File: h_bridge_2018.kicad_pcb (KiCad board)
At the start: 2 copper layers, 12 parts, among them J1 U$4, J2 Alim puissance, J7 PWM input, U1 LMD18200

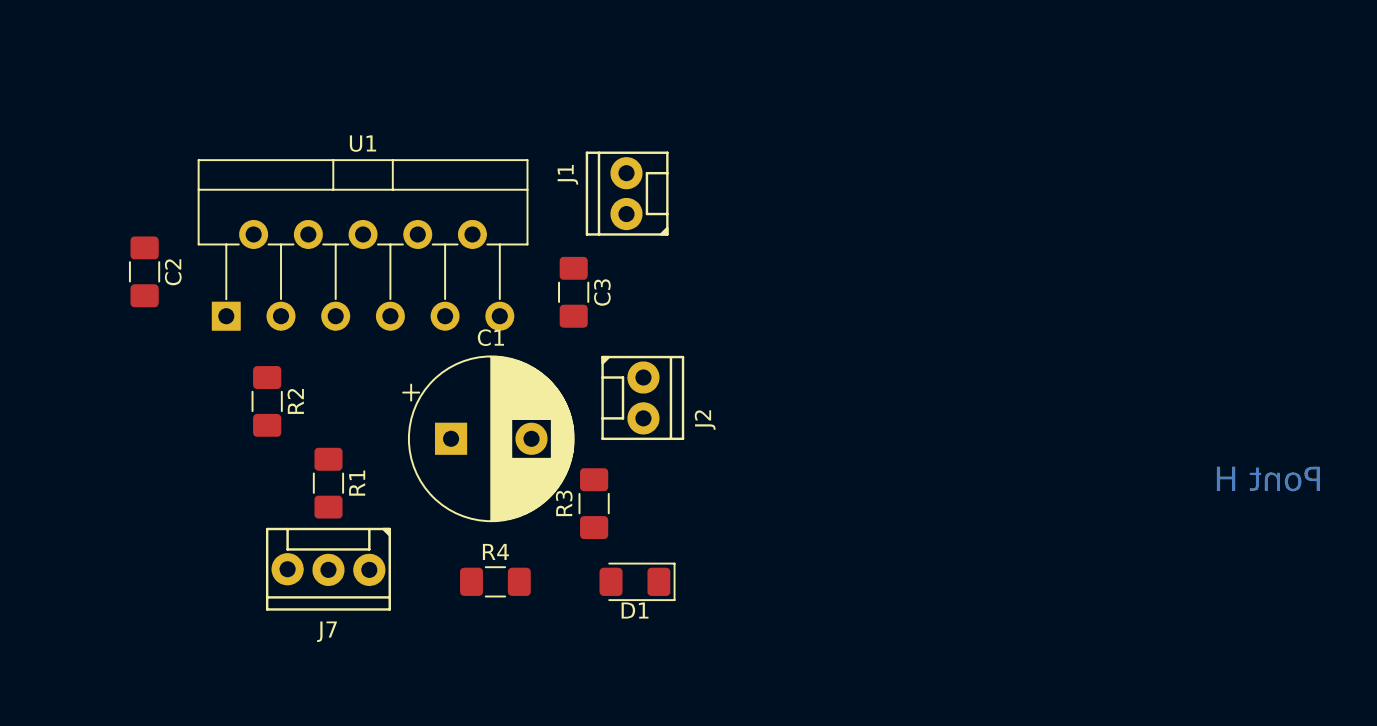
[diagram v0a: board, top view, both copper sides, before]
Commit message: h_bridge modified version
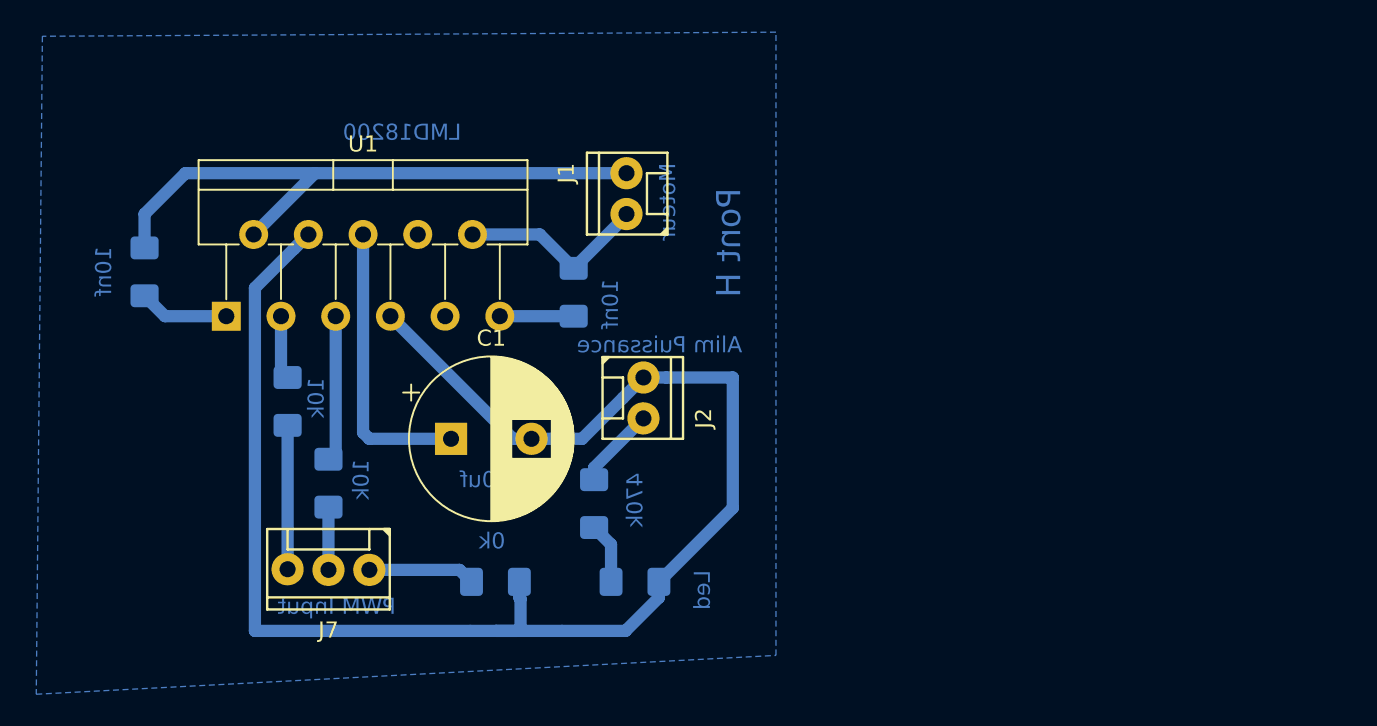
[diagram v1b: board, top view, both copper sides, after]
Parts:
- C2, C3, D1, R1, R2, R3, R4: moved to B.Cu
- moved R2 1.27 mm to (144.8, 84.0)
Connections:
- C1 pad 1: (no net) -> Net-(C1-Pad1)
- C1 pad 2: (no net) -> GNDPWR
- C2 pad 1: (no net) -> Net-(C2-Pad1)
- C2 pad 2: (no net) -> Net-(C2-Pad2)
- C3 pad 1: (no net) -> Net-(C3-Pad1)
- C3 pad 2: (no net) -> Net-(C3-Pad2)
- D1 pad 1: (no net) -> GNDPWR
- D1 pad 2: (no net) -> Net-(D1-Pad2)
- J1 pad 1: (no net) -> Net-(C3-Pad1)
- J1 pad 2: (no net) -> Net-(C2-Pad1)
- J2 pad 1: (no net) -> GNDPWR
- J2 pad 2: (no net) -> /VS
- J7 pad 1: (no net) -> Net-(J7-Pad1)
- J7 pad 2: (no net) -> Net-(J7-Pad2)
- J7 pad 3: (no net) -> Net-(J7-Pad3)
- R1 pad 1: (no net) -> Net-(R1-Pad1)
- R1 pad 2: (no net) -> Net-(J7-Pad2)
- R2 pad 1: (no net) -> Net-(R2-Pad1)
- R2 pad 2: (no net) -> Net-(J7-Pad3)
- R3 pad 1: (no net) -> Net-(D1-Pad2)
- R3 pad 2: (no net) -> /VS
- R4 pad 1: (no net) -> Net-(J7-Pad1)
- R4 pad 2: (no net) -> GNDPWR
- U1 pad 1: (no net) -> Net-(C2-Pad2)
- U1 pad 10: (no net) -> Net-(C3-Pad1)
- U1 pad 11: (no net) -> Net-(C3-Pad2)
- U1 pad 2: (no net) -> Net-(C2-Pad1)
- U1 pad 3: (no net) -> Net-(R2-Pad1)
- U1 pad 4: (no net) -> GNDPWR
- U1 pad 5: (no net) -> Net-(R1-Pad1)
- U1 pad 6: (no net) -> Net-(C1-Pad1)
- U1 pad 7: (no net) -> GNDPWR
- U1 pad 8: (no net) -> Net-(U1-Pad8)
- U1 pad 9: (no net) -> Net-(U1-Pad9)
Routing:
- net GNDPWR: track 0.00 -> 99.2 mm
- net Net-(C2-Pad1): track 0.00 -> 38.5 mm
- net Net-(C1-Pad1): track 0.00 -> 17.9 mm
- net Net-(C3-Pad1): track 0.00 -> 13.1 mm
- net Net-(R1-Pad1): track 0.00 -> 9.08 mm
- net Net-(J7-Pad3): track 0.00 -> 8.94 mm
- net Net-(J7-Pad1): track 0.00 -> 6.66 mm
- net Net-(C2-Pad2): track 0.00 -> 5.61 mm
- net /VS: track 0.00 -> 5.08 mm
- net Net-(C3-Pad2): track 0.00 -> 4.59 mm
- net Net-(R2-Pad1): track 0.00 -> 3.98 mm
- net Net-(J7-Pad2): track 0.00 -> 3.90 mm
- net Net-(D1-Pad2): track 0.00 -> 3.81 mm
- added copper zone on B.Cu, net GNDPWR
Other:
- board text added: "0k"
- board text added: "10k"
- board text added: "10nf"
- board text added: "470k"
- board text added: "470uf"
- board text added: "Alim Puissance"
- board text added: "LMD18200"
- board text added: "Led"
- board text added: "Moteur"
- board text added: "PWM Input"

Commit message: Update h_bridge_2018.kicad_pcb
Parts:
- moved C1 1.27 mm to (154.9, 85.1)
- moved C2 1.20 mm to (137.1, 76.0)
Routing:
- net GNDPWR: track 99.2 -> 102.2 mm
- net Net-(C2-Pad2): track 5.61 -> 4.40 mm
- net Net-(C1-Pad1): track 17.9 -> 16.9 mm
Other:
- board text removed: "0k"
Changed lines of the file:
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@@
   (general
     (thickness 1.6)
-    (drawings 13)
+    (drawings 12)
     (tracks 52)
     (zones 0)
@@
   )
   (module Capacitor_SMD:C_1206_3216Metric_Pad1.42x1.75mm_HandSolder (layer B.Cu)
-    (at 135.89 75.9825 270)
+    (at 137.09396 75.99172 270)
     (descr "Capacitor SMD 1206 (3216 Metric), square (rectangular) end terminal, IPC_7351 nominal with elongated pad for handsoldering. (Body size source: http://www.tortai-tech.com/upload/download/2011102023233369053.pdf), generated with kicad-footprint-generator")
     (tags "capacitor handsolder")
@@
   )
   (module Capacitor_THT:CP_Radial_D10.0mm_P5.00mm (layer F.Cu)
-    (at 154.94 86.36)
+    (at 154.94 85.09)
     (descr "CP, Radial series, Radial, pin pitch=5.00mm, , diameter=10mm, Electrolytic Capacitor")
     (tags "CP Radial series Radial pin pitch 5.00mm  diameter 10mm Electrolytic Capacitor")
@@
     )
   )
-  (gr_text Moteur (at 168.402 71.628 90) (layer B.Cu)
-    (effects (font (size 1 1) (thickness 0.1)) (justify mirror))
-  )
-  (gr_text "470k\n" (at 166.37 90.17 90) (layer B.Cu)
-    (effects (font (size 1 1) (thickness 0.1)) (justify mirror))
-  )
-  (gr_text "0k\n" (at 157.48 92.71) (layer B.Cu)
-    (effects (font (size 1 1) (thickness 0.1)) (justify mirror))
-  )
-  (gr_text "Led " (at 170.561 95.758 90) (layer B.Cu)
-    (effects (font (size 1 1) (thickness 0.1)) (justify mirror))
-  )
-  (gr_text "Alim Puissance" (at 167.894 80.518) (layer B.Cu)
-    (effects (font (size 1 1) (thickness 0.1)) (justify mirror))
-  )
-  (gr_text 10nf (at 164.846 77.978 90) (layer B.Cu)
-    (effects (font (size 1 1) (thickness 0.1)) (justify mirror))
-  )
-  (gr_text "10nf\n" (at 133.35 75.946 90) (layer B.Cu)
-    (effects (font (size 1 1) (thickness 0.1)) (justify mirror))
-  )
-  (gr_text "10k\n" (at 149.352 88.9 90) (layer B.Cu)
+  (gr_text Moteur (at 168.91 71.12 90) (layer B.Cu)
+    (effects (font (size 1 1) (thickness 0.1)) (justify mirror))
+  )
+  (gr_text "470k\n" (at 167.005 90.17 90) (layer B.Cu)
+    (effects (font (size 1 1) (thickness 0.1)) (justify mirror))
+  )
+  (gr_text "Led " (at 170.815 95.758 90) (layer B.Cu)
+    (effects (font (size 1 1) (thickness 0.1)) (justify mirror))
+  )
+  (gr_text "Alim Puissance" (at 175.26 86.36 90) (layer B.Cu)
+    (effects (font (size 1 1) (thickness 0.1)) (justify mirror))
+  )
+  (gr_text 10nf (at 166.37 77.25156 90) (layer B.Cu)
+    (effects (font (size 1 1) (thickness 0.1)) (justify mirror))
+  )
+  (gr_text "10nf\n" (at 133.985 76.01712 90) (layer B.Cu)
+    (effects (font (size 1 1) (thickness 0.1)) (justify mirror))
+  )
+  (gr_text "10k\n" (at 150.495 88.9 90) (layer B.Cu)
     (effects (font (size 1 1) (thickness 0.1)) (justify mirror))
   )
@@
     (effects (font (size 1 1) (thickness 0.1)) (justify mirror))
   )
-  (gr_text 470uf (at 157.48 88.9) (layer B.Cu)
-    (effects (font (size 1 1) (thickness 0.1)) (justify mirror))
-  )
-  (gr_text "LMD18200\n" (at 151.892 67.31) (layer B.Cu)
-    (effects (font (size 1 1) (thickness 0.1)) (justify mirror))
-  )
-  (gr_text "Pont H" (at 172.212 74.168 90) (layer B.Cu)
+  (gr_text 470uf (at 157.48 88.265) (layer B.Cu)
+    (effects (font (size 1 1) (thickness 0.1)) (justify mirror))
+  )
+  (gr_text "LMD18200\n" (at 153.53284 67.31) (layer B.Cu)
+    (effects (font (size 1 1) (thickness 0.1)) (justify mirror))
+  )
+  (gr_text "Pont H" (at 172.72 74.10704 90) (layer B.Cu)
     (effects (font (size 1.5 1.5) (thickness 0.3)) (justify mirror))
   )
-  (segment (start 156.27 73.66) (end 157.48 73.66) (width 0.25) (layer B.Cu) (net 5))
-  (segment (start 147.77 87.18) (end 147.32 87.63) (width 0.762) (layer B.Cu) (net 12))
-  (segment (start 147.77 78.74) (end 147.77 87.18) (width 0.762) (layer B.Cu) (net 12))
-  (segment (start 147.32 90.605) (end 147.32 94.506253) (width 0.762) (layer B.Cu) (net 10))
-  (segment (start 146.48 69.85) (end 142.67 73.66) (width 0.762) (layer B.Cu) (net 4))
-  (segment (start 165.843747 69.85) (end 146.48 69.85) (width 0.762) (layer B.Cu) (net 4))
-  (segment (start 157.97 78.74) (end 162.56 78.74) (width 0.762) (layer B.Cu) (net 6))
-  (segment (start 160.455 73.66) (end 162.56 75.765) (width 0.762) (layer B.Cu) (net 5))
-  (segment (start 156.27 73.66) (end 160.455 73.66) (width 0.762) (layer B.Cu) (net 5))
-  (segment (start 165.843747 72.481253) (end 162.56 75.765) (width 0.762) (layer B.Cu) (net 5))
-  (segment (start 165.843747 72.39) (end 165.843747 72.481253) (width 0.762) (layer B.Cu) (net 5))
-  (segment (start 137.16 78.74) (end 135.89 77.47) (width 0.762) (layer B.Cu) (net 3))
-  (segment (start 140.97 78.74) (end 137.16 78.74) (width 0.762) (layer B.Cu) (net 3))
-  (segment (start 135.89 74.495) (end 135.89 72.39) (width 0.762) (layer B.Cu) (net 4))
-  (segment (start 138.43 69.85) (end 146.48 69.85) (width 0.762) (layer B.Cu) (net 4))
-  (segment (start 135.89 72.39) (end 138.43 69.85) (width 0.762) (layer B.Cu) (net 4))
-  (segment (start 155.466253 94.506253) (end 156.21 95.25) (width 0.762) (layer B.Cu) (net 9))
-  (segment (start 149.86 94.506253) (end 155.466253 94.506253) (width 0.762) (layer B.Cu) (net 9))
-  (segment (start 149.47 73.66) (end 149.47 85.97) (width 0.762) (layer B.Cu) (net 2))
-  (segment (start 149.86 86.36) (end 154.94 86.36) (width 0.762) (layer B.Cu) (net 2))
-  (segment (start 149.47 85.97) (end 149.86 86.36) (width 0.762) (layer B.Cu) (net 2))
-  (segment (start 158.79 86.36) (end 159.94 86.36) (width 0.762) (layer B.Cu) (net 1))
-  (segment (start 151.17 78.74) (end 158.79 86.36) (width 0.762) (layer B.Cu) (net 1))
-  (segment (start 159.94 86.36) (end 163.086253 86.36) (width 0.762) (layer B.Cu) (net 1))
   (segment (start 165.626253 83.82) (end 166.896253 82.55) (width 0.762) (layer B.Cu) (net 1))
-  (segment (start 163.086253 86.36) (end 165.626253 83.82) (width 0.762) (layer B.Cu) (net 1))
-  (segment (start 163.83 88.156253) (end 166.896253 85.09) (width 0.762) (layer B.Cu) (net 8))
-  (segment (start 163.83 88.9) (end 163.83 88.156253) (width 0.762) (layer B.Cu) (net 8))
-  (segment (start 144.37 82.14) (end 144.78 82.55) (width 0.762) (layer B.Cu) (net 13))
-  (segment (start 144.37 78.74) (end 144.37 82.14) (width 0.762) (layer B.Cu) (net 13))
-  (segment (start 144.78 85.525) (end 144.78 94.466253) (width 0.762) (layer B.Cu) (net 11))
   (segment (start 145.170001 74.559999) (end 145.150001 74.559999) (width 0.762) (layer B.Cu) (net 1))
   (segment (start 146.07 73.66) (end 145.170001 74.559999) (width 0.762) (layer B.Cu) (net 1))
@@
   (segment (start 167.8575 96.225) (end 165.7845 98.298) (width 0.762) (layer B.Cu) (net 1))
   (segment (start 167.8575 95.25) (end 167.8575 96.225) (width 0.762) (layer B.Cu) (net 1))
+  (segment (start 151.17 78.74) (end 151.17 82.51) (width 0.762) (layer B.Cu) (net 1))
+  (segment (start 157.36 82.51) (end 159.94 85.09) (width 0.762) (layer B.Cu) (net 1))
+  (segment (start 151.17 82.51) (end 157.36 82.51) (width 0.762) (layer B.Cu) (net 1))
+  (segment (start 164.356253 85.09) (end 166.896253 82.55) (width 0.762) (layer B.Cu) (net 1))
+  (segment (start 159.94 85.09) (end 164.356253 85.09) (width 0.762) (layer B.Cu) (net 1))
+  (segment (start 149.47 85.09) (end 154.94 85.09) (width 0.762) (layer B.Cu) (net 2))
+  (segment (start 149.47 73.66) (end 149.47 85.09) (width 0.762) (layer B.Cu) (net 2))
+  (segment (start 139.70922 77.47922) (end 140.97 78.74) (width 0.762) (layer B.Cu) (net 3))
+  (segment (start 137.09396 77.47922) (end 139.70922 77.47922) (width 0.762) (layer B.Cu) (net 3))
+  (segment (start 146.48 69.85) (end 142.67 73.66) (width 0.762) (layer B.Cu) (net 4))
+  (segment (start 165.843747 69.85) (end 146.48 69.85) (width 0.762) (layer B.Cu) (net 4))
+  (segment (start 138.43 69.85) (end 146.48 69.85) (width 0.762) (layer B.Cu) (net 4))
+  (segment (start 137.09396 74.50422) (end 137.09396 71.18604) (width 0.762) (layer B.Cu) (net 4))
+  (segment (start 137.09396 71.18604) (end 138.43 69.85) (width 0.762) (layer B.Cu) (net 4))
+  (segment (start 156.27 73.66) (end 157.48 73.66) (width 0.25) (layer B.Cu) (net 5))
+  (segment (start 160.455 73.66) (end 162.56 75.765) (width 0.762) (layer B.Cu) (net 5))
+  (segment (start 156.27 73.66) (end 160.455 73.66) (width 0.762) (layer B.Cu) (net 5))
+  (segment (start 165.843747 72.481253) (end 162.56 75.765) (width 0.762) (layer B.Cu) (net 5))
+  (segment (start 165.843747 72.39) (end 165.843747 72.481253) (width 0.762) (layer B.Cu) (net 5))
+  (segment (start 157.97 78.74) (end 162.56 78.74) (width 0.762) (layer B.Cu) (net 6))
   (segment (start 164.8825 92.9275) (end 163.83 91.875) (width 0.762) (layer B.Cu) (net 7))
   (segment (start 164.8825 95.25) (end 164.8825 92.9275) (width 0.762) (layer B.Cu) (net 7))
+  (segment (start 163.83 88.156253) (end 166.896253 85.09) (width 0.762) (layer B.Cu) (net 8))
+  (segment (start 163.83 88.9) (end 163.83 88.156253) (width 0.762) (layer B.Cu) (net 8))
+  (segment (start 155.466253 94.506253) (end 156.21 95.25) (width 0.762) (layer B.Cu) (net 9))
+  (segment (start 149.86 94.506253) (end 155.466253 94.506253) (width 0.762) (layer B.Cu) (net 9))
+  (segment (start 147.32 90.605) (end 147.32 94.506253) (width 0.762) (layer B.Cu) (net 10))
+  (segment (start 144.78 85.525) (end 144.78 94.466253) (width 0.762) (layer B.Cu) (net 11))
+  (segment (start 147.77 87.18) (end 147.32 87.63) (width 0.762) (layer B.Cu) (net 12))
+  (segment (start 147.77 78.74) (end 147.77 87.18) (width 0.762) (layer B.Cu) (net 12))
+  (segment (start 144.37 82.14) (end 144.78 82.55) (width 0.762) (layer B.Cu) (net 13))
+  (segment (start 144.37 78.74) (end 144.37 82.14) (width 0.762) (layer B.Cu) (net 13))
   (zone (net 1) (net_name GNDPWR) (layer B.Cu) (hatch edge 0.508)
     (connect_pads (clearance 0.508))
@@
     (polygon
       (pts
-        (xy 175.133 99.822) (xy 175.133 61.087) (xy 129.54 61.341) (xy 129.159 102.235)
+        (xy 177.8 63.5) (xy 177.8 101.6) (xy 128.905 101.6) (xy 128.905 63.5)
       )
     )
